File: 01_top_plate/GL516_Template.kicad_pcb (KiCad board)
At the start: 2 copper layers, 314.4 x 98.8 mm, 58 parts, among them J10 Conn_01x01, J11 Conn_01x01, J12 Conn_01x01, J13 Conn_01x01, J14 Conn_01x01, J15 Conn_01x01, J16 Conn_01x01, J17 Conn_01x01, J2 Conn_01x01, J3 Conn_01x01, J4 Conn_01x01, J5 Conn_01x01, J6 Conn_01x01, J7 Conn_01x01, J8 Conn_01x01, J9 Conn_01x01, SW1 KEY_SWITCH, SW10 KEY_SWITCH, SW11 KEY_SWITCH, SW12 KEY_SWITCH, SW13 KEY_SWITCH, SW14 KEY_SWITCH, SW15 KEY_SWITCH, SW16 KEY_SWITCH, SW17 KEY_SWITCH, SW18 KEY_SWITCH, SW19 KEY_SWITCH, SW2 KEY_SWITCH, SW20 KEY_SWITCH, SW21 KEY_SWITCH, SW22 KEY_SWITCH, SW23 KEY_SWITCH, SW24 KEY_SWITCH, SW25 KEY_SWITCH, SW26 KEY_SWITCH, SW27 KEY_SWITCH, SW28 KEY_SWITCH, SW29 KEY_SWITCH, SW3 KEY_SWITCH, SW30 KEY_SWITCH, SW31 KEY_SWITCH, SW32 KEY_SWITCH, SW33 KEY_SWITCH, SW34 KEY_SWITCH, SW35 KEY_SWITCH, SW36 KEY_SWITCH, SW37 KEY_SWITCH, SW38 KEY_SWITCH, SW39 KEY_SWITCH, SW4 KEY_SWITCH, SW40 KEY_SWITCH, SW41 KEY_SWITCH, SW42 KEY_SWITCH, SW5 KEY_SWITCH, SW6 KEY_SWITCH, SW7 KEY_SWITCH, SW8 KEY_SWITCH, SW9 KEY_SWITCH

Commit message: Top Plate Nuri-tsubushi and logo
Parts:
- added G***: LOGO, logo:kuzumo_logo_mask.kicad_mod_20per, F.Cu at (171.4, 62.8)
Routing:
- added copper zone on F.Cu, net (none)

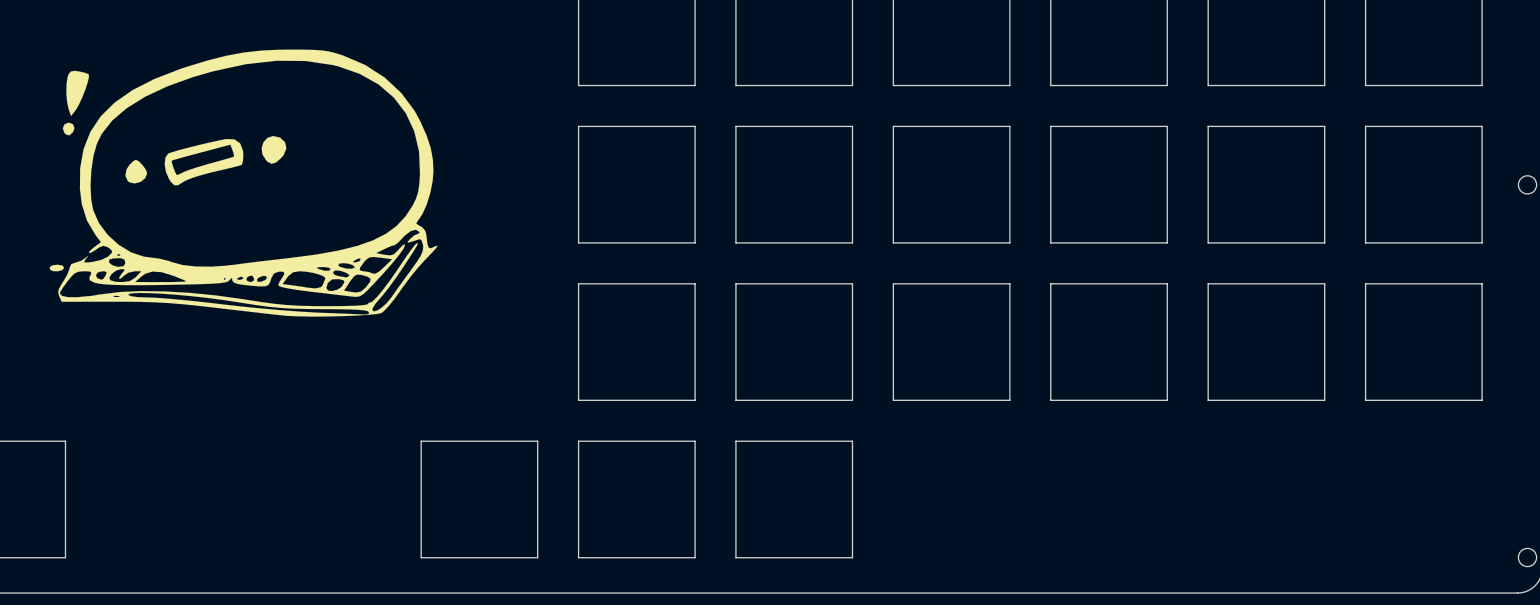
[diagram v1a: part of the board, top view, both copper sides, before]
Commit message: fix logo on Top Plate
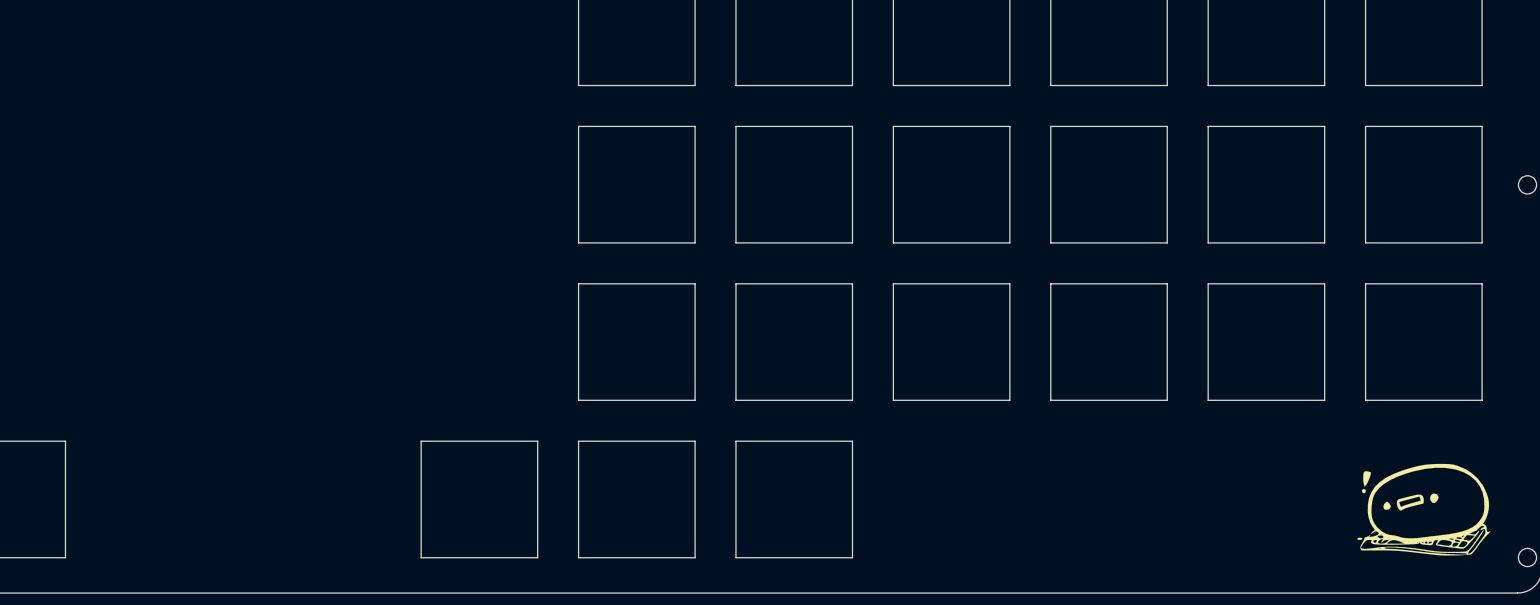
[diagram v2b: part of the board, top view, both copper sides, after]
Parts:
- removed the G*** at (171.4, 62.8)
- added G***: LOGO, logos:kuzumotchi_logo_mask_mini, F.Cu at (314.3, 104.7)

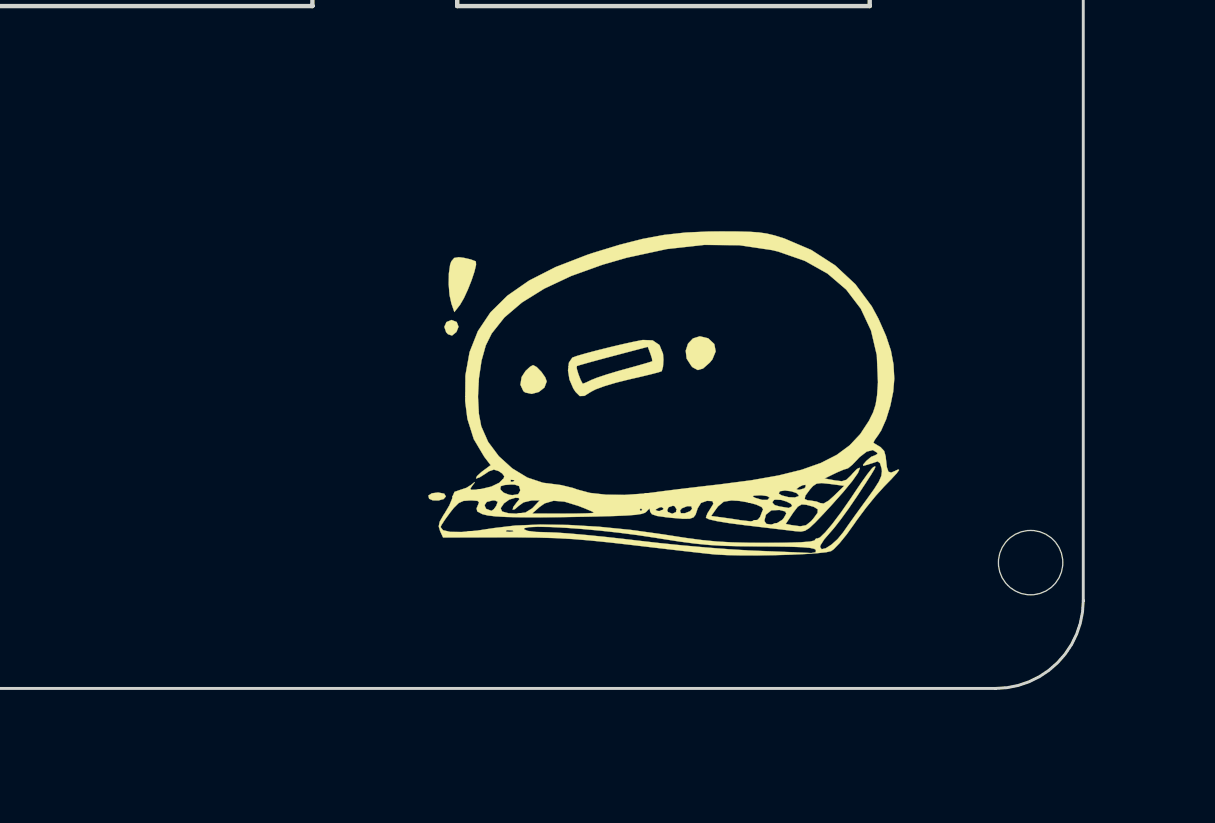
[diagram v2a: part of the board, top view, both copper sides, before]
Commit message: add version text on both Top and Assembly Plates
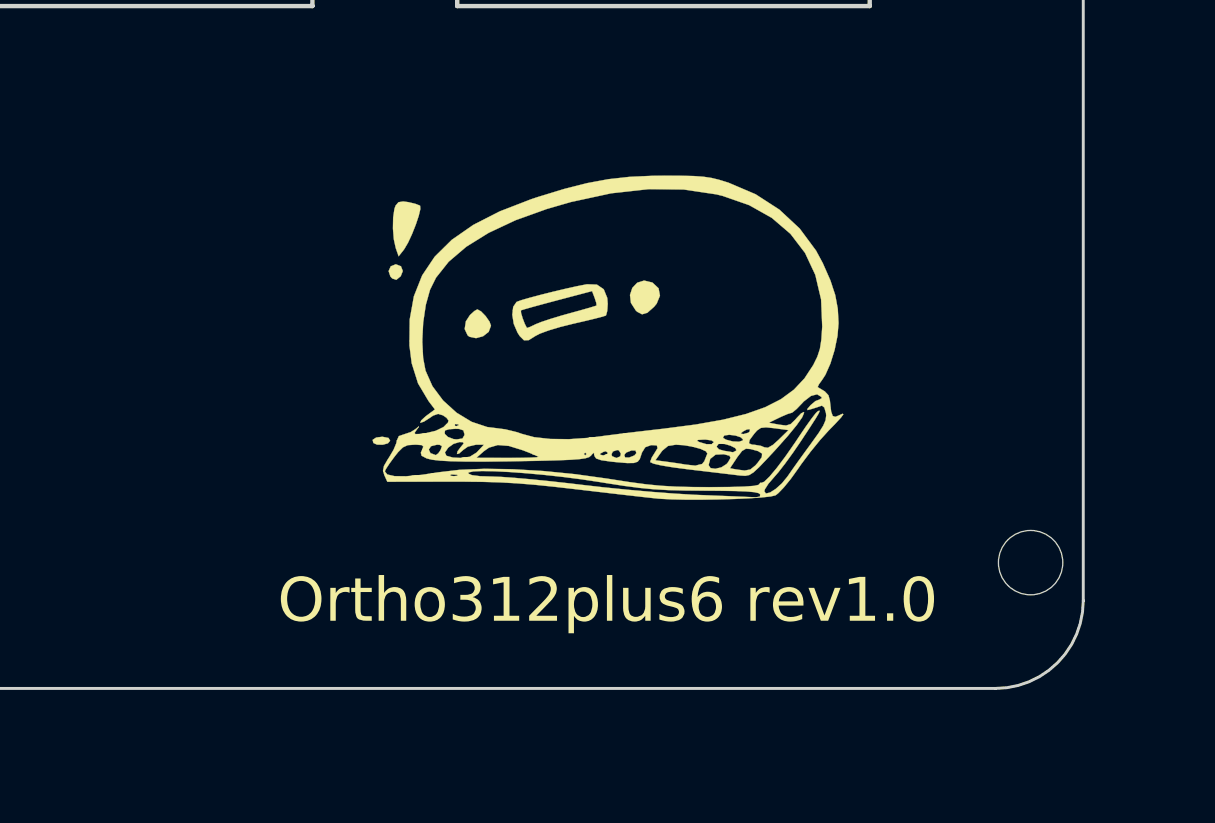
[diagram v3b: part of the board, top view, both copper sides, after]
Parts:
- moved G*** 2.69 mm to (312.4, 102.8)
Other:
- board text added: "Ortho312plus6 rev1.0"
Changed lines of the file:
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@@
   (general
     (thickness 1.6)
-    (drawings 730)
+    (drawings 731)
     (tracks 0)
     (zones 0)
@@
   )
   (module logos:kuzumotchi_logo_mask_mini (layer F.Cu)
-    (at 314.275 104.725)
+    (at 312.37 102.82)
     (fp_text reference G*** (at 0 0) (layer F.SilkS) hide
       (effects (font (size 1.524 1.524) (thickness 0.3)))
@@
     )
   )
+  (gr_text "Ortho312plus6 rev1.0\n\n" (at 312.37 114.25) (layer F.SilkS)
+    (effects (font (size 1.5 1.5) (thickness 0.3)))
+  )
   (gr_arc (start 302.225 92.674999) (end 302.225 92.674999) (angle -90) (layer Dwgs.User) (width 0.2))

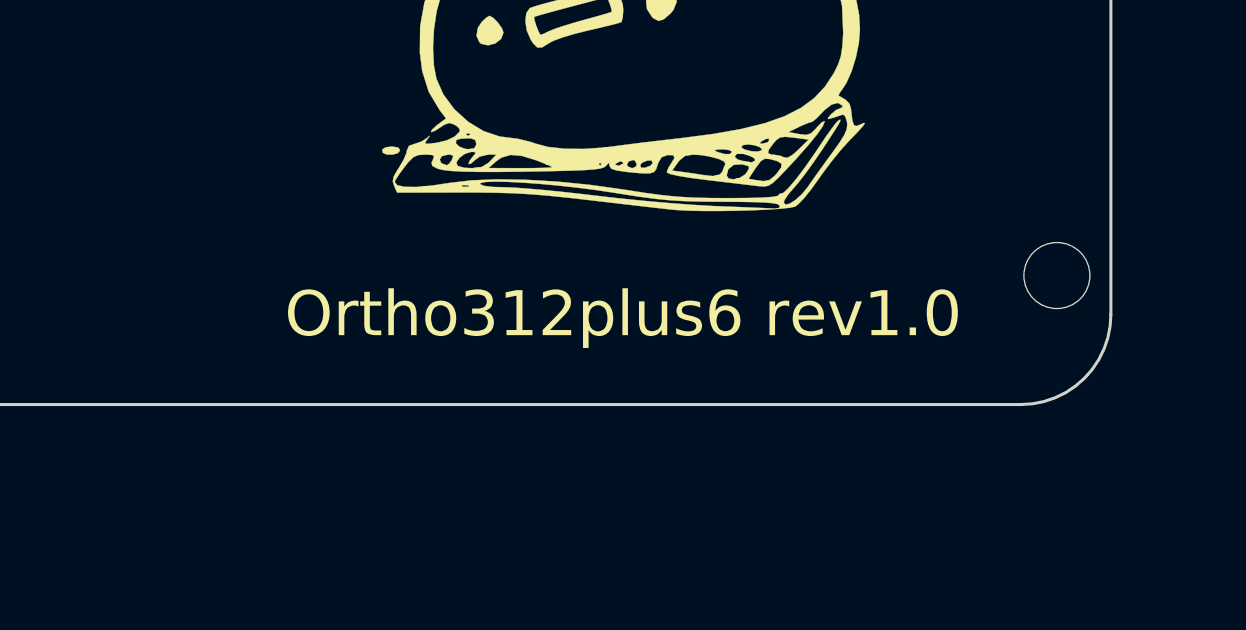
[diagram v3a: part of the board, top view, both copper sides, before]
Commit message: add battery + - silk / mod version
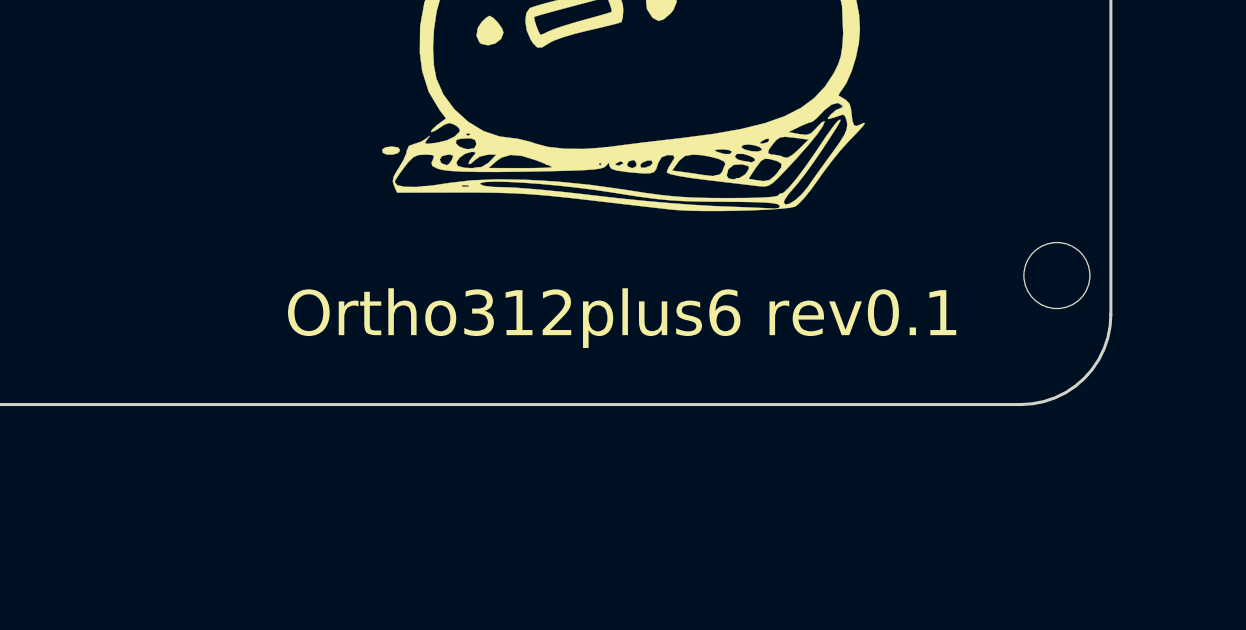
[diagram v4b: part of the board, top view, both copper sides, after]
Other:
- board text added: "Ortho312plus6 rev0.1"
- board text removed: "Ortho312plus6 rev1.0"
